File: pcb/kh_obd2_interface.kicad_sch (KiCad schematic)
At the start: 1 part, among them J1 OBD2

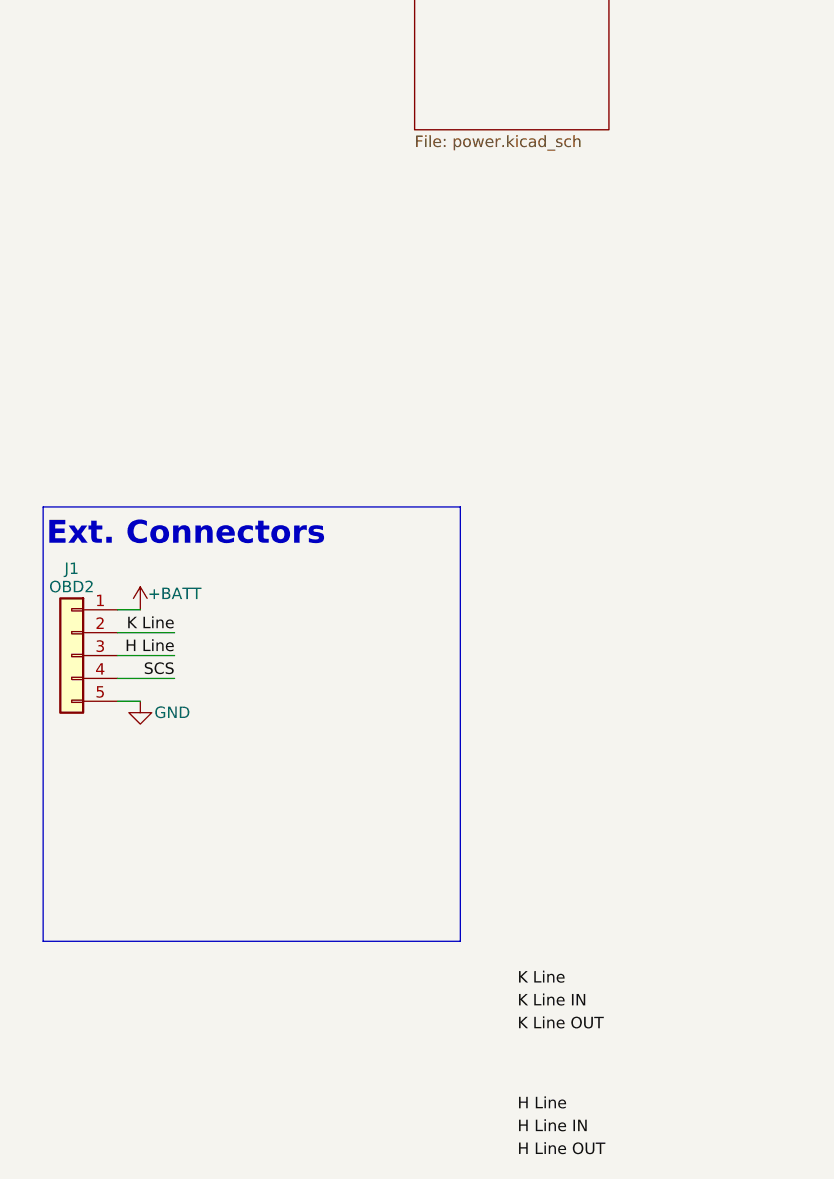
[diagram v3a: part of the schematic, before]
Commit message: add connectors schem
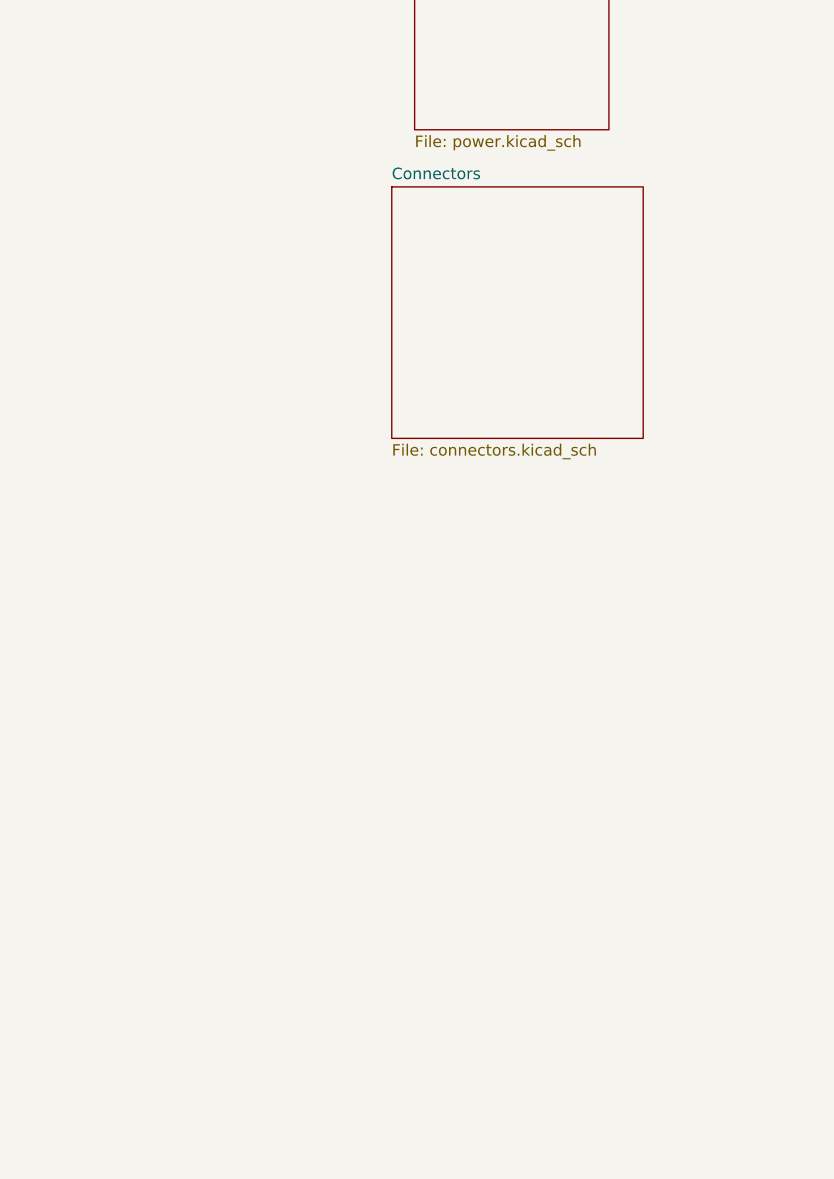
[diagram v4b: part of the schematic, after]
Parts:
- removed J1: OBD2, Connector_Molex:Molex_SL_171971-0004_1x04_P2.54mm_Vertical, symbol Connector_Generic:Conn_01x05
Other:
- added sheet Connectors (connectors.kicad_sch)
- note removed: "Ext. Connectors"

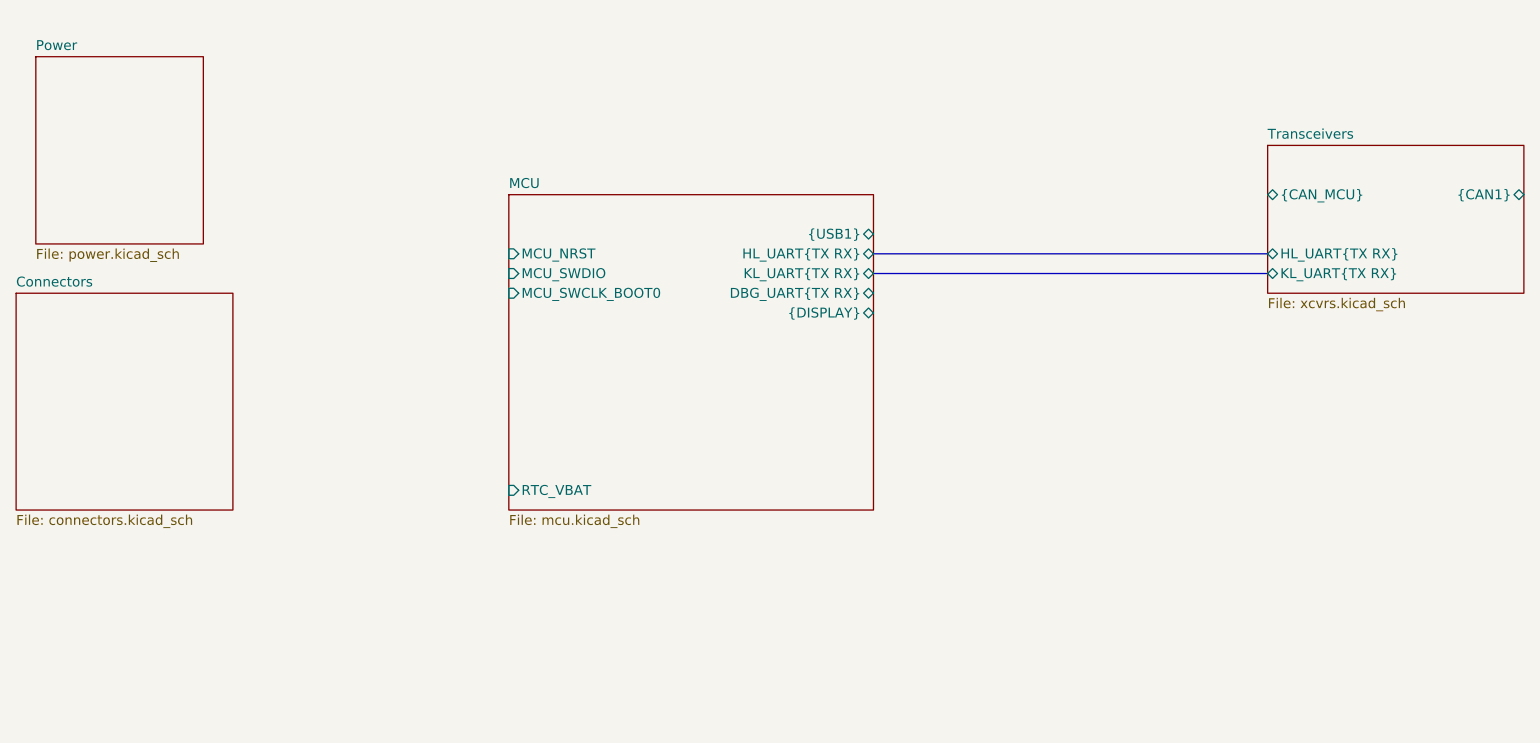
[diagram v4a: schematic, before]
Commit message: add transceivers, routing, drc
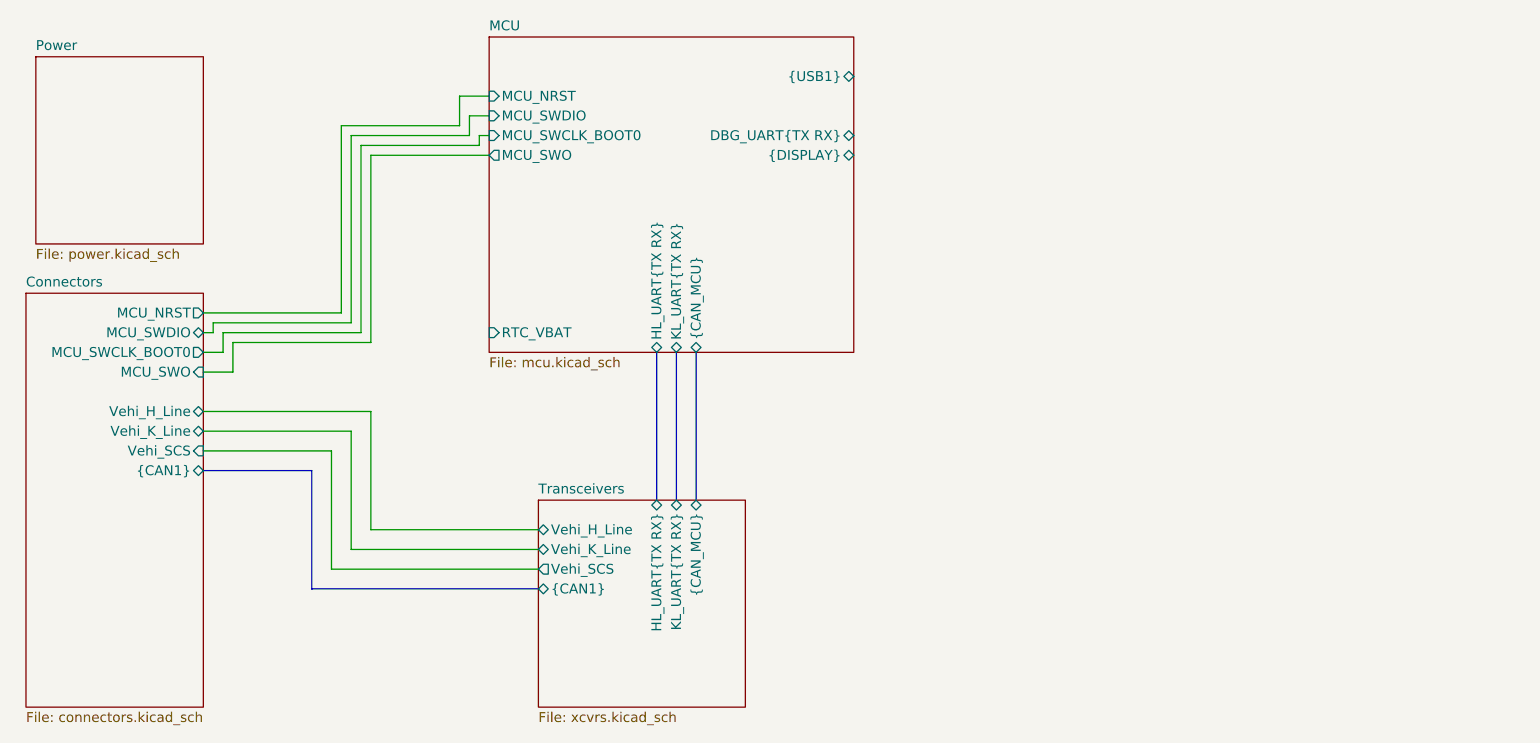
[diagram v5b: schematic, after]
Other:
- sheet Connectors ports: added MCU_NRST, MCU_SWCLK_BOOT0, MCU_SWDIO, MCU_SWO, Vehi_H_Line, Vehi_K_Line, Vehi_SCS, {CAN1}; removed none
- sheet MCU ports: added MCU_SWO, {CAN_MCU}; removed none
- sheet Transceivers ports: added Vehi_H_Line, Vehi_K_Line, Vehi_SCS; removed none

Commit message: busses are hard
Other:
- sheet Connectors ports: added RTC_VBAT, USB_5V, {CAN}, {USB}; removed {CAN1}
- sheet MCU ports: added DISPLAY{DISPLAY}, HLINE{UART}, KLINE{UART}, {USB}; removed HL_UART{TX RX}, KL_UART{TX RX}, {DISPLAY}, {USB1}
- sheet Power ports: added USB_5V; removed none
- sheet Transceivers ports: added HLINE{UART}, KLINE{UART}, {CAN}; removed HL_UART{TX RX}, KL_UART{TX RX}, {CAN1}
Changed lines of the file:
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@@
 	(bus
 		(pts
-			(xy 74.93 85.09) (xy 88.9 85.09)
+			(xy 74.93 91.44) (xy 88.9 91.44)
 		)
 		(stroke
@@
 	(wire
 		(pts
+			(xy 106.68 67.31) (xy 111.76 67.31)
+		)
+		(stroke
+			(width 0)
+			(type default)
+		)
+	)
+	(wire
+		(pts
 			(xy 107.95 40.64) (xy 107.95 36.83)
 		)
@@
 		)
 	)
+	(bus
+		(pts
+			(xy 104.14 59.69) (xy 111.76 59.69)
+		)
+		(stroke
+			(width 0)
+			(type default)
+		)
+	)
 	(wire
 		(pts
@@
 	(wire
 		(pts
-			(xy 74.93 82.55) (xy 91.44 82.55)
+			(xy 74.93 88.9) (xy 91.44 88.9)
 		)
 		(stroke
@@
 		)
 	)
+	(wire
+		(pts
+			(xy 74.93 80.01) (xy 106.68 80.01)
+		)
+		(stroke
+			(width 0)
+			(type default)
+		)
+	)
 	(bus
 		(pts
-			(xy 88.9 85.09) (xy 88.9 100.33)
+			(xy 88.9 91.44) (xy 88.9 100.33)
 		)
 		(stroke
@@
 		)
 	)
+	(bus
+		(pts
+			(xy 74.93 76.2) (xy 104.14 76.2)
+		)
+		(stroke
+			(width 0)
+			(type default)
+		)
+	)
 	(wire
 		(pts
@@
 	(wire
 		(pts
+			(xy 48.26 52.07) (xy 52.07 52.07)
+		)
+		(stroke
+			(width 0)
+			(type default)
+		)
+	)
+	(wire
+		(pts
 			(xy 107.95 36.83) (xy 111.76 36.83)
 		)
@@
 	(wire
 		(pts
-			(xy 91.44 82.55) (xy 91.44 97.79)
+			(xy 91.44 88.9) (xy 91.44 97.79)
 		)
 		(stroke
@@
 	(wire
 		(pts
-			(xy 96.52 77.47) (xy 96.52 92.71)
+			(xy 96.52 83.82) (xy 96.52 92.71)
+		)
+		(stroke
+			(width 0)
+			(type default)
+		)
+	)
+	(wire
+		(pts
+			(xy 106.68 67.31) (xy 106.68 80.01)
 		)
 		(stroke
@@
 	(wire
 		(pts
-			(xy 74.93 77.47) (xy 96.52 77.47)
+			(xy 74.93 83.82) (xy 96.52 83.82)
 		)
 		(stroke
@@
 	(wire
 		(pts
-			(xy 93.98 80.01) (xy 93.98 95.25)
+			(xy 93.98 86.36) (xy 93.98 95.25)
+		)
+		(stroke
+			(width 0)
+			(type default)
+		)
+	)
+	(bus
+		(pts
+			(xy 104.14 59.69) (xy 104.14 76.2)
 		)
 		(stroke
@@
 	(wire
 		(pts
+			(xy 48.26 64.77) (xy 52.07 64.77)
+		)
+		(stroke
+			(width 0)
+			(type default)
+		)
+	)
+	(wire
+		(pts
 			(xy 78.74 68.58) (xy 96.52 68.58)
 		)
@@
 	(wire
 		(pts
+			(xy 48.26 52.07) (xy 48.26 64.77)
+		)
+		(stroke
+			(width 0)
+			(type default)
+		)
+	)
+	(wire
+		(pts
 			(xy 95.25 43.18) (xy 110.49 43.18)
 		)
@@
 	(wire
 		(pts
-			(xy 74.93 80.01) (xy 93.98 80.01)
+			(xy 74.93 86.36) (xy 93.98 86.36)
 		)
 		(stroke
@@
 		)
 		(pin "Vehi_H_Line" bidirectional
-			(at 74.93 77.47 0)
+			(at 74.93 83.82 0)
 			(effects
 				(font
@@
 		)
 		(pin "Vehi_K_Line" bidirectional
-			(at 74.93 80.01 0)
+			(at 74.93 86.36 0)
 			(effects
 				(font
@@
 		)
 		(pin "Vehi_SCS" input
-			(at 74.93 82.55 0)
-			(effects
-				(font
-					(size 1.27 1.27)
-				)
-				(justify right)
-			)
-		)
-		(pin "{CAN1}" bidirectional
-			(at 74.93 85.09 0)
+			(at 74.93 88.9 0)
+			(effects
+				(font
+					(size 1.27 1.27)
+				)
+				(justify right)
+			)
+		)
+		(pin "{CAN}" bidirectional
+			(at 74.93 91.44 0)
 			(effects
 				(font
@@
 		(pin "MCU_SWO" input
 			(at 74.93 72.39 0)
+			(effects
+				(font
+					(size 1.27 1.27)
+				)
+				(justify right)
+			)
+		)
+		(pin "USB_5V" output
+			(at 52.07 64.77 180)
+			(effects
+				(font
+					(size 1.27 1.27)
+				)
+				(justify left)
+			)
+		)
+		(pin "RTC_VBAT" output
+			(at 74.93 80.01 0)
+			(effects
+				(font
+					(size 1.27 1.27)
+				)
+				(justify right)
+			)
+		)
+		(pin "{USB}" output
+			(at 74.93 76.2 0)
 			(effects
 				(font
@@
 	)
 	(sheet
-		(at 53.34 31.75)
-		(size 21.59 24.13)
+		(at 52.07 49.53)
+		(size 22.86 5.08)
 		(exclude_from_sim no)
 		(in_bom yes)
@@
 		)
 		(property "Sheetname" "Power"
-			(at 53.34 31.0384 0)
+			(at 52.07 48.8184 0)
 			(effects
 				(font
@@
 		)
 		(property "Sheetfile" "power.kicad_sch"
-			(at 53.34 56.4646 0)
+			(at 52.07 55.1946 0)
 			(effects
 				(font
@@
 				)
 				(justify left top)
+			)
+		)
+		(pin "USB_5V" input
+			(at 52.07 52.07 180)
+			(effects
+				(font
+					(size 1.27 1.27)
+				)
+				(justify left)
 			)
 		)
@@
 			)
 		)
-		(pin "KL_UART{TX RX}" bidirectional
+		(pin "KLINE{UART}" bidirectional
 			(at 135.89 88.9 90)
 			(effects
@@
 			)
 		)
-		(pin "HL_UART{TX RX}" bidirectional
+		(pin "HLINE{UART}" bidirectional
 			(at 133.35 88.9 90)
 			(effects
@@
 			)
 		)
-		(pin "{CAN1}" bidirectional
+		(pin "{CAN}" bidirectional
 			(at 118.11 100.33 180)
 			(effects
@@
 			)
 		)
-		(pin "HL_UART{TX RX}" bidirectional
+		(pin "HLINE{UART}" bidirectional
 			(at 133.35 69.85 270)
 			(effects
@@
 			)
 		)
-		(pin "KL_UART{TX RX}" bidirectional
+		(pin "KLINE{UART}" bidirectional
 			(at 135.89 69.85 270)
 			(effects
@@
 			)
 		)
-		(pin "{DISPLAY}" bidirectional
+		(pin "DISPLAY{DISPLAY}" bidirectional
 			(at 158.75 44.45 0)
-			(effects
-				(font
-					(size 1.27 1.27)
-				)
-				(justify right)
-			)
-		)
-		(pin "{USB1}" bidirectional
-			(at 158.75 34.29 0)
 			(effects
 				(font
@@
 			(effects
 				(font
+					(size 1.27 1.27)
+				)
+				(justify left)
+			)
+		)
+		(pin "{USB}" input
+			(at 111.76 59.69 180)
+			(effects
+				(font

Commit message: Add TLIN2027, placement, DRC fixes, routing
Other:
- sheet Transceivers renamed Communications
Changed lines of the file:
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@@
 			(color 0 0 0 0.0000)
 		)
-		(property "Sheetname" "Transceivers"
+		(property "Sheetname" "Communications"
 			(at 118.11 88.1884 0)
 			(effects

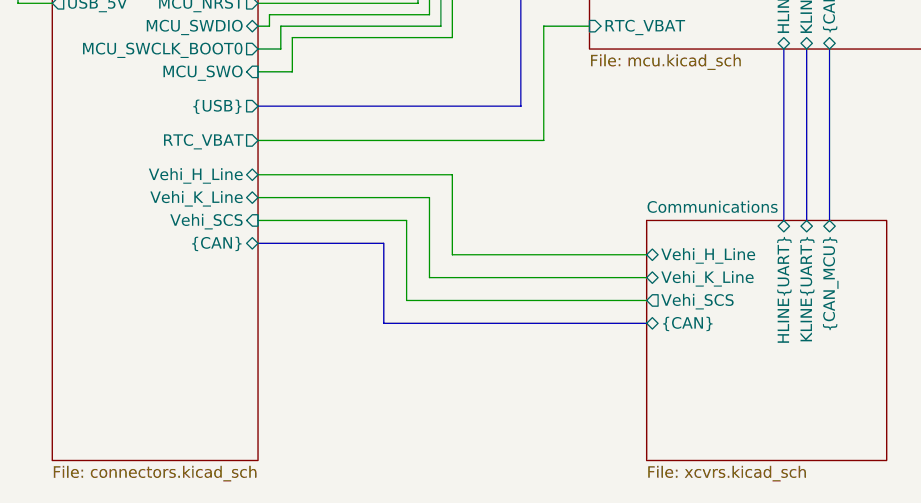
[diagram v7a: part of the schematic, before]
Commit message: CAN/mcu placement/routing
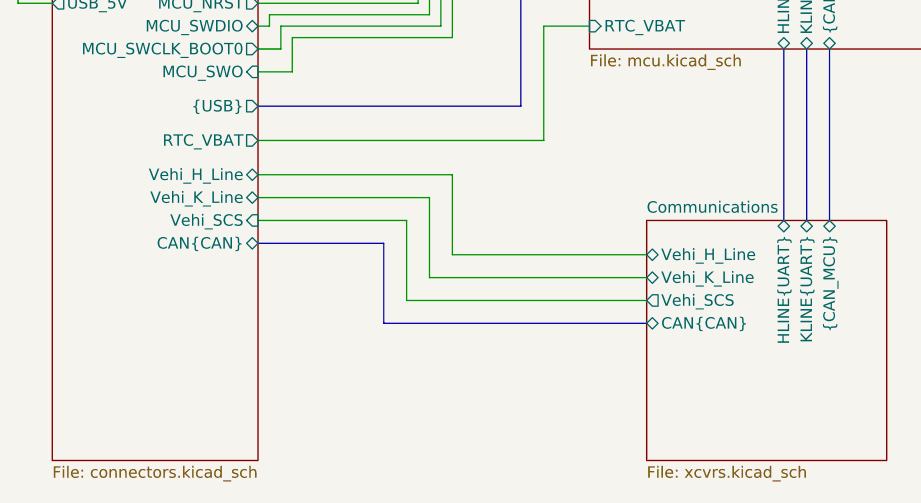
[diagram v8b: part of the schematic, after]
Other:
- sheet Communications ports: added CAN{CAN}; removed {CAN}
- sheet Connectors ports: added CAN{CAN}; removed {CAN}
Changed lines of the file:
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@@
 			)
 		)
-		(pin "{CAN}" bidirectional
+		(pin "CAN{CAN}" bidirectional
 			(at 74.93 91.44 0)
 			(effects
@@
 			)
 		)
-		(pin "{CAN}" bidirectional
+		(pin "CAN{CAN}" bidirectional
 			(at 118.11 100.33 180)
 			(effects
